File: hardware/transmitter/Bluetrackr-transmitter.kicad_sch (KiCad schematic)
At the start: 57 parts, among them J1 USB_C_Receptacle_USB2.0, J2 Programming_Connector, J3 Battery_Connector, Q1 CJ2333, Q2 BSS138, Q3 BSS138, Q4 BSS138, Q5 BSS138, Q6 BSS138, SW1 SW_Pair, U1 MCP73831-2-OT, U2 MIC5205-3.3YM5, U3 MCP1700-1802E_SOT23, U4 STM32F030R8Tx, U5 NRF24L01_Breakout, U6 ICM-20948

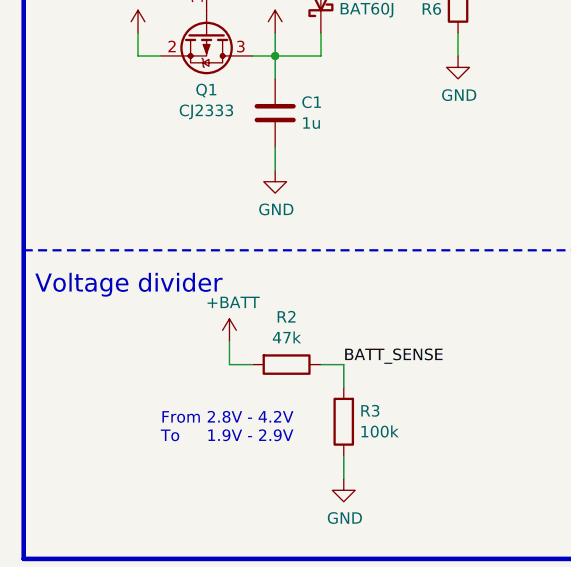
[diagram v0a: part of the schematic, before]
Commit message: Remove changelog for now
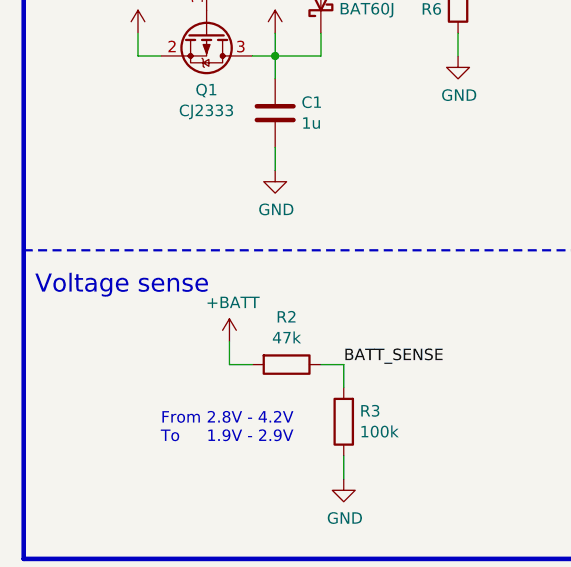
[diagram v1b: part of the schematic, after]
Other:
- note added: "Voltage sense"
- note removed: "Voltage divider"
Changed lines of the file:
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@@
     (effects (font (size 2 2)) (justify left bottom))
   )
-  (text "Voltage divider" (at 26.67 214.63 0)
+  (text "Voltage sense" (at 26.67 214.63 0)
     (effects (font (size 2 2)) (justify left bottom))
   )

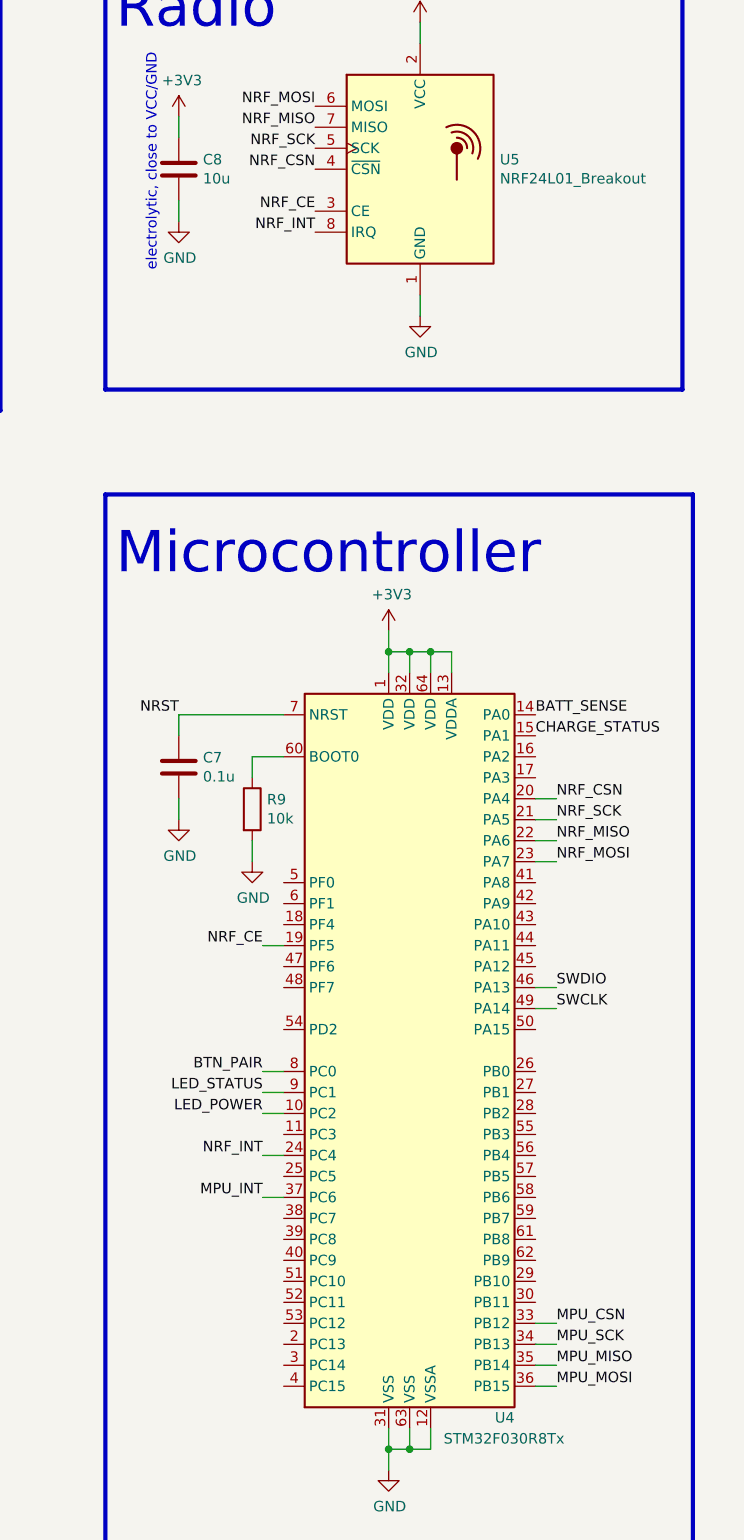
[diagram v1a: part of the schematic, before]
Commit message: Fix not connected errors on ERC
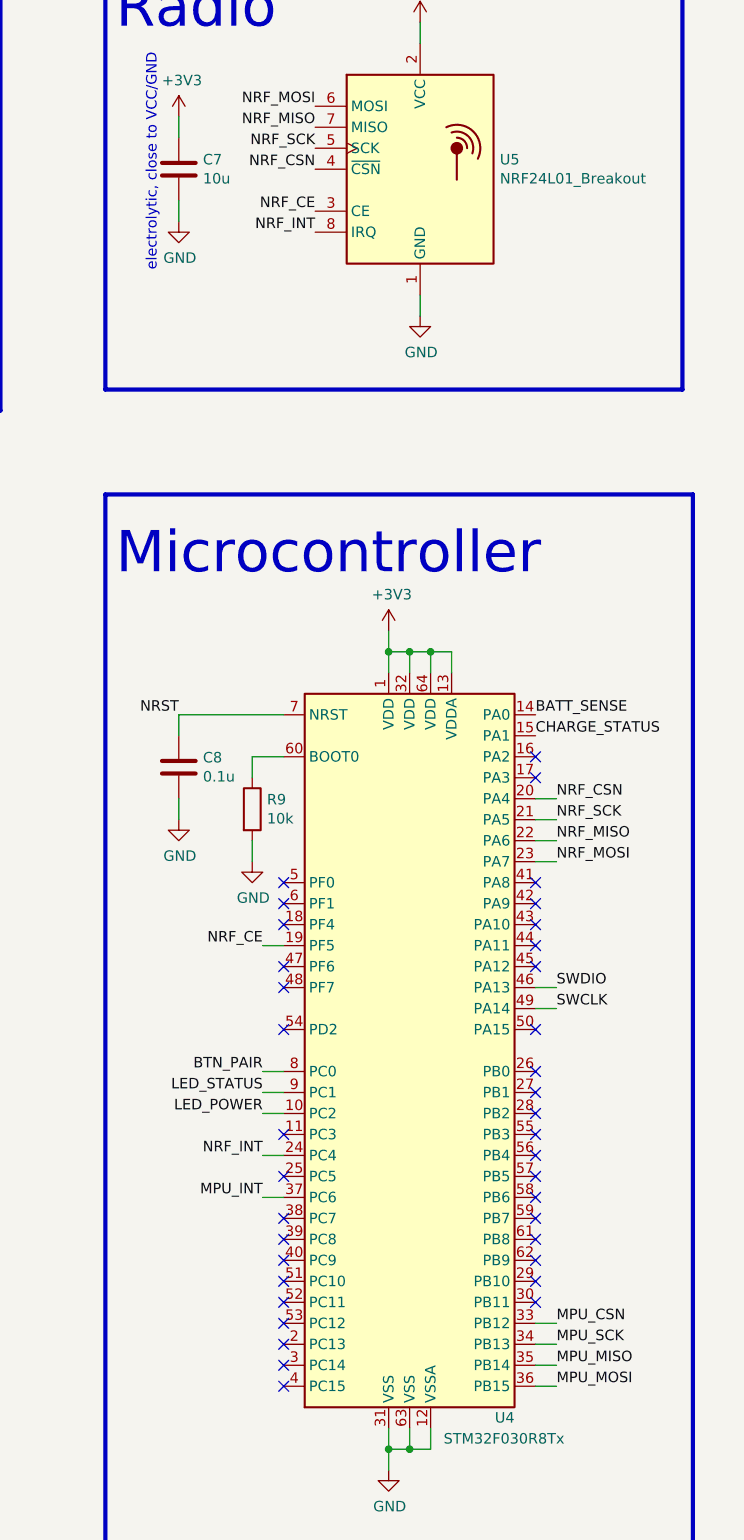
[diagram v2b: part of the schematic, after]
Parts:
- renumbered C8 to C7, C7 to C8
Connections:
- no-connect marks 9 -> 46
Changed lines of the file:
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@@
   (no_connect (at 325.12 57.15))
   (no_connect (at 299.72 62.23))
+  (no_connect (at 217.17 138.43))
+  (no_connect (at 217.17 140.97))
+  (no_connect (at 217.17 143.51))
+  (no_connect (at 217.17 148.59))
+  (no_connect (at 217.17 151.13))
+  (no_connect (at 217.17 156.21))
+  (no_connect (at 217.17 168.91))
+  (no_connect (at 217.17 173.99))
+  (no_connect (at 217.17 179.07))
+  (no_connect (at 217.17 181.61))
+  (no_connect (at 217.17 184.15))
+  (no_connect (at 217.17 186.69))
+  (no_connect (at 217.17 189.23))
+  (no_connect (at 217.17 191.77))
+  (no_connect (at 217.17 194.31))
+  (no_connect (at 217.17 196.85))
+  (no_connect (at 217.17 199.39))
+  (no_connect (at 247.65 123.19))
+  (no_connect (at 247.65 125.73))
+  (no_connect (at 247.65 138.43))
+  (no_connect (at 247.65 140.97))
+  (no_connect (at 247.65 143.51))
+  (no_connect (at 247.65 146.05))
+  (no_connect (at 247.65 148.59))
+  (no_connect (at 247.65 156.21))
+  (no_connect (at 247.65 161.29))
+  (no_connect (at 247.65 163.83))
+  (no_connect (at 247.65 166.37))
+  (no_connect (at 247.65 168.91))
+  (no_connect (at 247.65 171.45))
+  (no_connect (at 247.65 173.99))
+  (no_connect (at 247.65 176.53))
+  (no_connect (at 247.65 179.07))
+  (no_connect (at 247.65 181.61))
+  (no_connect (at 247.65 184.15))
+  (no_connect (at 247.65 186.69))
+  (no_connect (at 247.65 189.23))
   (no_connect (at 54.61 58.42))
   (wire (pts (xy 31.75 83.82) (xy 31.75 86.36))
@@
   )
   (symbol (lib_id "power:PWR_FLAG") (at 336.55 215.9 180) (unit 1)
-    (property "Reference" "#FLG?" (id 0) (at 336.55 217.805 0)
+    (property "Reference" "#FLG01" (id 0) (at 336.55 217.805 0)
       (effects (font (size 1.27 1.27)) hide)
     )
@@
   )
   (symbol (lib_id "power:PWR_FLAG") (at 346.71 215.9 180) (unit 1)
-    (property "Reference" "#FLG0102" (id 0) (at 346.71 217.805 0)
+    (property "Reference" "#FLG02" (id 0) (at 346.71 217.805 0)
       (effects (font (size 1.27 1.27)) hide)
     )
@@
   )
   (symbol (lib_id "power:PWR_FLAG") (at 356.87 213.36 0) (unit 1)
-    (property "Reference" "#FLG0101" (id 0) (at 356.87 211.455 0)
+    (property "Reference" "#FLG03" (id 0) (at 356.87 211.455 0)
       (effects (font (size 1.27 1.27)) hide)
     )
@@
   )
   (symbol (lib_id "power:+BATT") (at 106.68 73.66 0) (unit 1)
-    (property "Reference" "#PWR0103" (id 0) (at 106.68 77.47 0)
+    (property "Reference" "#PWR018" (id 0) (at 106.68 77.47 0)
       (effects (font (size 1.27 1.27)) hide)
     )
@@
   )
   (symbol (lib_id "power:VCC") (at 106.68 130.81 0) (unit 1)
-    (property "Reference" "#PWR018" (id 0) (at 106.68 134.62 0)
+    (property "Reference" "#PWR020" (id 0) (at 106.68 134.62 0)
       (effects (font (size 1.27 1.27)) hide)
     )
@@
   )
   (symbol (lib_id "power:+3V3") (at 204.47 45.72 0) (unit 1)
-    (property "Reference" "#PWR031" (id 0) (at 204.47 49.53 0)
+    (property "Reference" "#PWR030" (id 0) (at 204.47 49.53 0)
       (effects (font (size 1.27 1.27)) hide)
     )
@@
   )
   (symbol (lib_id "power:VCC") (at 336.55 213.36 0) (unit 1)
-    (property "Reference" "#PWR?" (id 0) (at 336.55 217.17 0)
+    (property "Reference" "#PWR049" (id 0) (at 336.55 217.17 0)
       (effects (font (size 1.27 1.27)) hide)
     )
@@
   )
   (symbol (lib_id "power:+1V8") (at 344.17 127 0) (unit 1)
-    (property "Reference" "#PWR049" (id 0) (at 344.17 130.81 0)
+    (property "Reference" "#PWR050" (id 0) (at 344.17 130.81 0)
       (effects (font (size 1.27 1.27)) hide)
     )
@@
   )
   (symbol (lib_id "power:+1V8") (at 344.17 158.75 0) (unit 1)
-    (property "Reference" "#PWR050" (id 0) (at 344.17 162.56 0)
+    (property "Reference" "#PWR051" (id 0) (at 344.17 162.56 0)
       (effects (font (size 1.27 1.27)) hide)
     )
@@
   )
   (symbol (lib_id "power:VBUS") (at 346.71 213.36 0) (unit 1)
-    (property "Reference" "#PWR?" (id 0) (at 346.71 217.17 0)
+    (property "Reference" "#PWR052" (id 0) (at 346.71 217.17 0)
       (effects (font (size 1.27 1.27)) hide)
     )
@@
   )
   (symbol (lib_id "power:+1V8") (at 349.25 48.26 0) (unit 1)
-    (property "Reference" "#PWR051" (id 0) (at 349.25 52.07 0)
+    (property "Reference" "#PWR053" (id 0) (at 349.25 52.07 0)
       (effects (font (size 1.27 1.27)) hide)
     )
@@
   )
   (symbol (lib_id "power:+3V3") (at 359.41 127 0) (unit 1)
-    (property "Reference" "#PWR053" (id 0) (at 359.41 130.81 0)
+    (property "Reference" "#PWR056" (id 0) (at 359.41 130.81 0)
       (effects (font (size 1.27 1.27)) hide)
     )
@@
   )
   (symbol (lib_id "power:+3V3") (at 359.41 158.75 0) (unit 1)
-    (property "Reference" "#PWR054" (id 0) (at 359.41 162.56 0)
+    (property "Reference" "#PWR057" (id 0) (at 359.41 162.56 0)
       (effects (font (size 1.27 1.27)) hide)
     )
@@
   )
   (symbol (lib_id "power:GND") (at 106.68 81.28 0) (unit 1)
-    (property "Reference" "#PWR020" (id 0) (at 106.68 87.63 0)
+    (property "Reference" "#PWR019" (id 0) (at 106.68 87.63 0)
       (effects (font (size 1.27 1.27)) hide)
     )
@@
   )
   (symbol (lib_id "power:GND") (at 204.47 58.42 0) (unit 1)
-    (property "Reference" "#PWR032" (id 0) (at 204.47 64.77 0)
+    (property "Reference" "#PWR031" (id 0) (at 204.47 64.77 0)
       (effects (font (size 1.27 1.27)) hide)
     )
@@
   )
   (symbol (lib_id "power:GND") (at 204.47 130.81 0) (unit 1)
-    (property "Reference" "#PWR030" (id 0) (at 204.47 137.16 0)
+    (property "Reference" "#PWR032" (id 0) (at 204.47 137.16 0)
       (effects (font (size 1.27 1.27)) hide)
     )
@@
   )
   (symbol (lib_id "power:GND") (at 349.25 66.04 0) (unit 1)
-    (property "Reference" "#PWR052" (id 0) (at 349.25 72.39 0)
+    (property "Reference" "#PWR054" (id 0) (at 349.25 72.39 0)
       (effects (font (size 1.27 1.27)) hide)
     )
@@
   )
   (symbol (lib_id "power:GND") (at 356.87 215.9 0) (unit 1)
-    (property "Reference" "#PWR0101" (id 0) (at 356.87 222.25 0)
+    (property "Reference" "#PWR055" (id 0) (at 356.87 222.25 0)
       (effects (font (size 1.27 1.27)) hide)
     )
@@
   )
   (symbol (lib_id "Device:C") (at 204.47 52.07 0) (unit 1)
-    (property "Reference" "C8" (id 0) (at 207.391 50.9016 0)
+    (property "Reference" "C7" (id 0) (at 207.391 50.9016 0)
       (effects (font (size 1.27 1.27)) (justify left))
     )
@@
   )
   (symbol (lib_id "Device:C") (at 204.47 124.46 0) (unit 1)
-    (property "Reference" "C7" (id 0) (at 207.391 123.2916 0)
+    (property "Reference" "C8" (id 0) (at 207.391 123.2916 0)
       (effects (font (size 1.27 1.27)) (justify left))
     )
@@
   )
   (symbol_instances
+    (path "/74614f0a-29d1-418f-88b8-e77369481dff"
+      (reference "#FLG01") (unit 1)
+    )
+    (path "/7b519107-9783-4e3c-923e-a04e141dd5fd"
+      (reference "#FLG02") (unit 1)
+    )
     (path "/4fda9896-3b56-4e89-b484-6ad9c0d1ec69"
-      (reference "#FLG0101") (unit 1)
-    )
-    (path "/7b519107-9783-4e3c-923e-a04e141dd5fd"
-      (reference "#FLG0102") (unit 1)
-    )
-    (path "/74614f0a-29d1-418f-88b8-e77369481dff"
-      (reference "#FLG?") (unit 1)
+      (reference "#FLG03") (unit 1)
     )
     (path "/00000000-0000-0000-0000-00005f04fcd4"
@@
       (reference "#PWR017") (unit 1)
     )
+    (path "/c8159ff4-4630-466c-b642-80860032c7cf"
+      (reference "#PWR018") (unit 1)
+    )
+    (path "/00000000-0000-0000-0000-00005e29cfdb"
+      (reference "#PWR019") (unit 1)
+    )
     (path "/00000000-0000-0000-0000-00005e239471"
-      (reference "#PWR018") (unit 1)
-    )
-    (path "/00000000-0000-0000-0000-00005e29cfdb"
       (reference "#PWR020") (unit 1)
     )
@@
       (reference "#PWR029") (unit 1)
     )
+    (path "/e811cb27-3761-400f-8d29-e25e81995bc3"
+      (reference "#PWR030") (unit 1)
+    )
+    (path "/03bc3a52-47d5-4713-b1bd-c9a8387cc555"
+      (reference "#PWR031") (unit 1)
+    )
     (path "/00000000-0000-0000-0000-00005eea291f"
-      (reference "#PWR030") (unit 1)
-    )
-    (path "/e811cb27-3761-400f-8d29-e25e81995bc3"
-      (reference "#PWR031") (unit 1)
-    )
-    (path "/03bc3a52-47d5-4713-b1bd-c9a8387cc555"
       (reference "#PWR032") (unit 1)
     )
@@
       (reference "#PWR048") (unit 1)
     )
+    (path "/ed7e11ed-6c1c-4d2d-ab25-a69e4a6d17b5"
+      (reference "#PWR049") (unit 1)
+    )
     (path "/00000000-0000-0000-0000-00005f5398e9"
-      (reference "#PWR049") (unit 1)
+      (reference "#PWR050") (unit 1)
     )
     (path "/00000000-0000-0000-0000-00005f51f0c6"
-      (reference "#PWR050") (unit 1)
+      (reference "#PWR051") (unit 1)
+    )
+    (path "/03815ab4-d07d-40a7-a6af-983919a4e904"
+      (reference "#PWR052") (unit 1)
     )
     (path "/c2d894f5-a002-44e5-b15f-1c4423b02fcb"
-      (reference "#PWR051") (unit 1)
+      (reference "#PWR053") (unit 1)
     )
     (path "/00000000-0000-0000-0000-00005f456027"
-      (reference "#PWR052") (unit 1)
+      (reference "#PWR054") (unit 1)
+    )
+    (path "/6312b39b-cde1-4abe-b153-1b2dcfd55fbd"
+      (reference "#PWR055") (unit 1)
     )
     (path "/00000000-0000-0000-0000-00005f5398f8"
-      (reference "#PWR053") (unit 1)
+      (reference "#PWR056") (unit 1)
     )
     (path "/00000000-0000-0000-0000-00005f51f0d5"
-      (reference "#PWR054") (unit 1)
-    )
-    (path "/6312b39b-cde1-4abe-b153-1b2dcfd55fbd"
-      (reference "#PWR0101") (unit 1)
-    )
-    (path "/c8159ff4-4630-466c-b642-80860032c7cf"
-      (reference "#PWR0103") (unit 1)
-    )
-    (path "/03815ab4-d07d-40a7-a6af-983919a4e904"
-      (reference "#PWR?") (unit 1)
-    )
-    (path "/ed7e11ed-6c1c-4d2d-ab25-a69e4a6d17b5"
-      (reference "#PWR?") (unit 1)
+      (reference "#PWR057") (unit 1)
     )
     (path "/00000000-0000-0000-0000-00005ed75ddf"
@@
       (reference "C6") (unit 1)
     )
+    (path "/00000000-0000-0000-0000-00005da70c62"
+      (reference "C7") (unit 1)
+    )
     (path "/00000000-0000-0000-0000-00005eea369a"
-      (reference "C7") (unit 1)
-    )
-    (path "/00000000-0000-0000-0000-00005da70c62"
       (reference "C8") (unit 1)
     )

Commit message: Add board basic dimensions 5x3cm
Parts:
- C1, C13, C14, C15, C5, C6, C8: footprint (none) -> Capacitor_SMD:C_0805_2012Metric_Pad1.15x1.40mm_HandSolder
- C7: footprint Capacitor_SMD:C_1206_3216Metric_Pad1.42x1.75mm_HandSolder -> Capacitor_SMD:CP_Elec_4x5.4
- J1: footprint Connector_USB:USB_C_Receptacle_HRO_TYPE-C-31-M-12 -> User_Connector_USB:USB_C_Receptacle_HRO_TYPE-C-31-M-12
- J2: footprint Connector_PinHeader_2.54mm:PinHeader_1x04_P2.54mm_Vertical -> Connector_JST:JST_XH_S4B-XH-A_1x04_P2.50mm_Horizontal
- J3: footprint Connector_PinHeader_2.54mm:PinHeader_1x02_P2.54mm_Vertical -> Connector_JST:JST_XH_B2B-XH-A_1x02_P2.50mm_Vertical
- R1, R10, R11, R12, R13, R14, R15, R16, R17, R18, R19, R4, R5: footprint (none) -> Resistor_SMD:R_0805_2012Metric_Pad1.15x1.40mm_HandSolder
